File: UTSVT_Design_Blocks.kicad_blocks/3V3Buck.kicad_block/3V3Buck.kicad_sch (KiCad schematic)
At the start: 8 parts, among them U1 LMR51635XDDCR

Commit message: review addressed
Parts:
- C3: P/N 963-T21GCB7225MTPA1J -> CL21F225ZAFNNNE
- C6, C7: P/N 963-MLAST32MAB5476MP -> GRM32ER61C476KE15L
- L1: footprint Inductor_SMD:L_Cenker_CKCS252010 -> Inductor_SMD:L_TDK_SLF6025; LCSC P/N C354546 -> C2997651; P/N 710-78439346056 -> PNLS6045-5R6M 5.6UH
- R6: P/N 652-CR0603FX-3162ELF -> 0603WAF3162T5E
- R7: P/N 603-RT0603DRE0710K2L -> 0603WAF1022T5E
- U1: P/N 595-LMR51635XDDCR -> LMR51635XDDCR
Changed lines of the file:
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@@
 			)
 		)
-		(property "P/N" "963-MLAST32MAB5476MP"
+		(property "P/N" "GRM32ER61C476KE15L"
 			(at 166.37 85.09 0)
 			(effects
@@
 			)
 		)
-		(property "P/N" "652-CR0603FX-3162ELF"
+		(property "P/N" "0603WAF3162T5E"
 			(at 201.93 82.55 0)
 			(effects
@@
 			)
 		)
-		(property "P/N" "963-MLAST32MAB5476MP"
+		(property "P/N" "GRM32ER61C476KE15L"
 			(at 154.94 85.09 0)
 			(effects
@@
 			)
 		)
-		(property "Footprint" "Inductor_SMD:L_Cenker_CKCS252010"
+		(property "Footprint" "Inductor_SMD:L_TDK_SLF6025"
 			(at 146.05 81.28 0)
 			(effects
@@
 			)
 		)
-		(property "LCSC P/N" "C354546"
+		(property "LCSC P/N" "C2997651"
 			(at 146.05 81.28 90)
 			(effects
@@
 			)
 		)
-		(property "P/N" "710-78439346056"
+		(property "P/N" "PNLS6045-5R6M 5.6UH"
 			(at 146.05 81.28 90)
 			(effects
@@
 			)
 		)
-		(property "P/N" "595-LMR51635XDDCR"
+		(property "P/N" "LMR51635XDDCR"
 			(at 97.79 76.2 0)
 			(effects
@@
 			)
 		)
-		(property "P/N" "963-T21GCB7225MTPA1J"
+		(property "P/N" "CL21F225ZAFNNNE"
 			(at 77.47 81.28 0)
 			(effects
@@
 			)
 		)
-		(property "P/N" "603-RT0603DRE0710K2L"
+		(property "P/N" "0603WAF1022T5E"
 			(at 201.93 90.17 0)
 			(effects

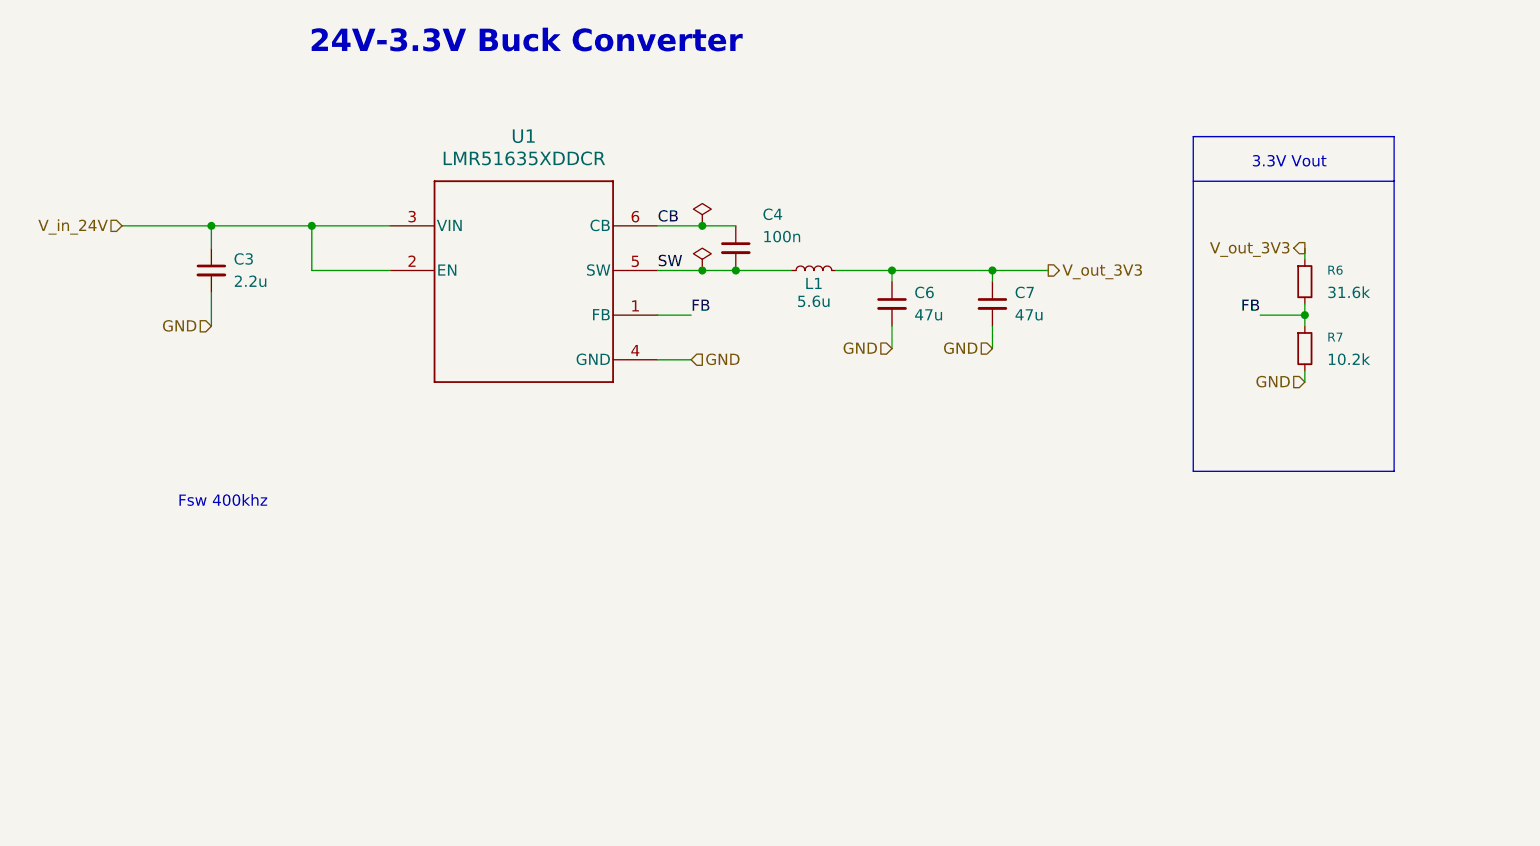
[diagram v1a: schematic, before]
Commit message: fixed designators
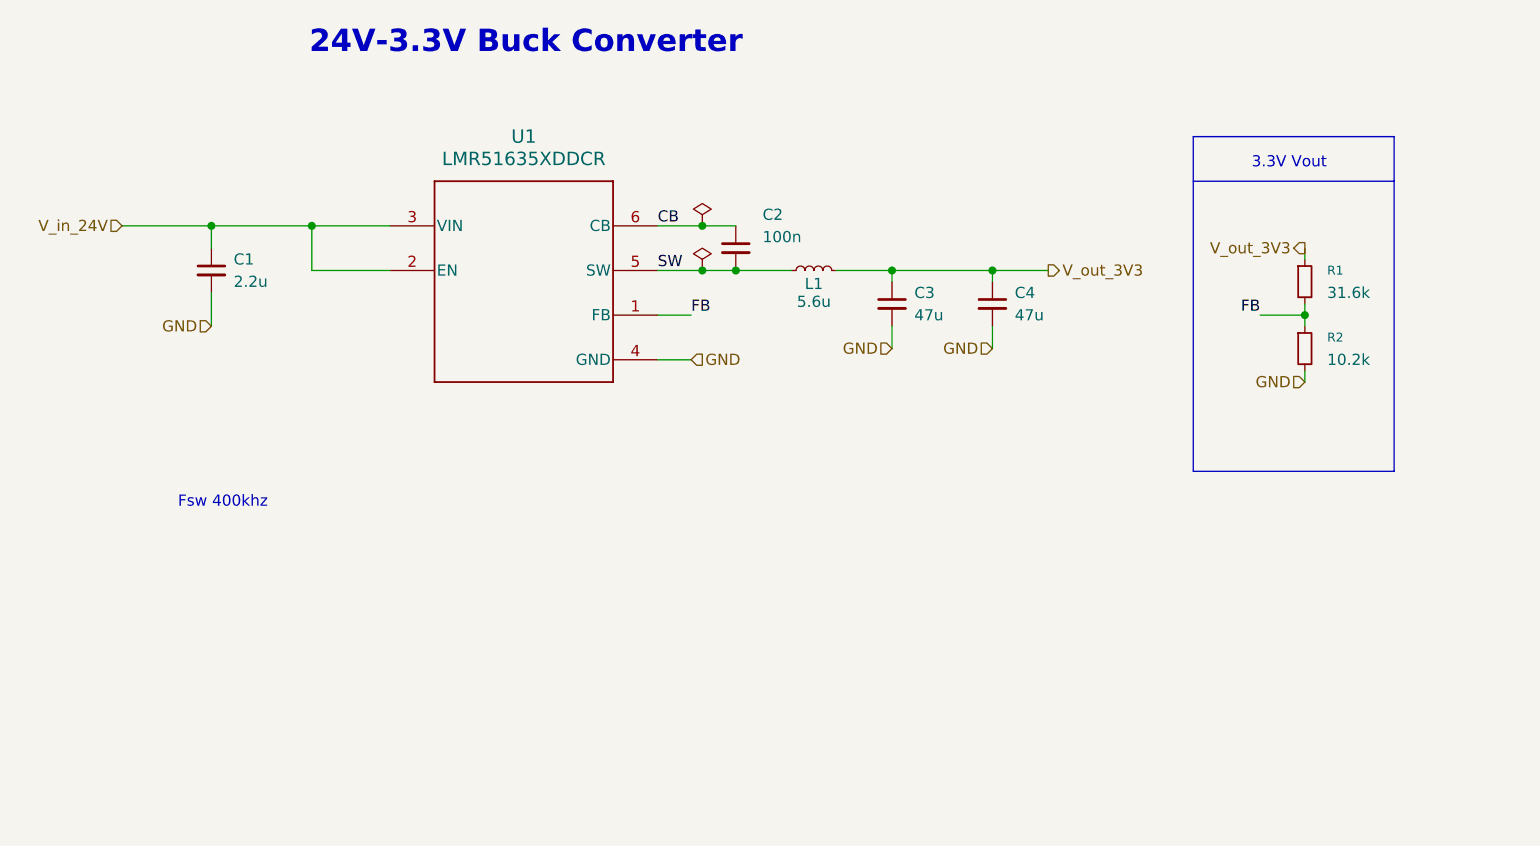
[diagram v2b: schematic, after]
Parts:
- renumbered C3 to C1, C4 to C2, C6 to C3, C7 to C4, R6 to R1, R7 to R2
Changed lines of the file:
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@@
 		(dnp no)
 		(fields_autoplaced yes)
-		(property "Reference" "C7"
+		(property "Reference" "C4"
 			(at 168.91 83.8262 0)
 			(effects
@@
 				(path "/331f457b-ed4e-4d4a-ad6d-c8acb2febfed/5a40936c-0191-464a-8f77-aefefe09d184"
 					(reference "C7")
+					(unit 1)
+				)
+			)
+			(project "3V3Buck"
+				(path "/39da07fa-d2fd-433c-a855-3c74e2086fee"
+					(reference "C4")
 					(unit 1)
 				)
@@
 		(dnp no)
 		(fields_autoplaced yes)
-		(property "Reference" "R6"
+		(property "Reference" "R1"
 			(at 204.47 81.2799 0)
 			(effects
@@
 				(path "/331f457b-ed4e-4d4a-ad6d-c8acb2febfed/5a40936c-0191-464a-8f77-aefefe09d184"
 					(reference "R6")
+					(unit 1)
+				)
+			)
+			(project "3V3Buck"
+				(path "/39da07fa-d2fd-433c-a855-3c74e2086fee"
+					(reference "R1")
 					(unit 1)
 				)
@@
 		(dnp no)
 		(fields_autoplaced yes)
-		(property "Reference" "C6"
+		(property "Reference" "C3"
 			(at 157.48 83.8262 0)
 			(effects
@@
 				(path "/331f457b-ed4e-4d4a-ad6d-c8acb2febfed/5a40936c-0191-464a-8f77-aefefe09d184"
 					(reference "C6")
+					(unit 1)
+				)
+			)
+			(project "3V3Buck"
+				(path "/39da07fa-d2fd-433c-a855-3c74e2086fee"
+					(reference "C3")
 					(unit 1)
 				)
@@
 		(dnp no)
 		(fields_autoplaced yes)
-		(property "Reference" "#FLG04"
+		(property "Reference" "#FLG01"
 			(at 133.35 74.295 0)
 			(effects
@@
 				(path "/331f457b-ed4e-4d4a-ad6d-c8acb2febfed/5a40936c-0191-464a-8f77-aefefe09d184"
 					(reference "#FLG04")
+					(unit 1)
+				)
+			)
+			(project "3V3Buck"
+				(path "/39da07fa-d2fd-433c-a855-3c74e2086fee"
+					(reference "#FLG01")
 					(unit 1)
 				)
@@
 				)
 			)
+			(project "3V3Buck"
+				(path "/39da07fa-d2fd-433c-a855-3c74e2086fee"
+					(reference "L1")
+					(unit 1)
+				)
+			)
 		)
 	)
@@
 				)
 			)
+			(project "3V3Buck"
+				(path "/39da07fa-d2fd-433c-a855-3c74e2086fee"
+					(reference "U1")
+					(unit 1)
+				)
+			)
 		)
 	)
@@
 		(dnp no)
 		(fields_autoplaced yes)
-		(property "Reference" "C3"
+		(property "Reference" "C1"
 			(at 80.01 80.0162 0)
 			(effects
@@
 				(path "/331f457b-ed4e-4d4a-ad6d-c8acb2febfed/5a40936c-0191-464a-8f77-aefefe09d184"
 					(reference "C3")
+					(unit 1)
+				)
+			)
+			(project "3V3Buck"
+				(path "/39da07fa-d2fd-433c-a855-3c74e2086fee"
+					(reference "C1")
 					(unit 1)
 				)
@@
 		(on_board yes)
 		(dnp no)
-		(property "Reference" "#FLG03"
+		(property "Reference" "#FLG02"
 			(at 133.35 79.375 0)
 			(effects
@@
 				(path "/331f457b-ed4e-4d4a-ad6d-c8acb2febfed/5a40936c-0191-464a-8f77-aefefe09d184"
 					(reference "#FLG03")
+					(unit 1)
+				)
+			)
+			(project "3V3Buck"
+				(path "/39da07fa-d2fd-433c-a855-3c74e2086fee"
+					(reference "#FLG02")
 					(unit 1)
 				)
@@
 		(on_board yes)
 		(dnp no)
-		(property "Reference" "C4"
+		(property "Reference" "C2"
 			(at 140.208 74.93 0)
 			(effects
@@
 				(path "/331f457b-ed4e-4d4a-ad6d-c8acb2febfed/5a40936c-0191-464a-8f77-aefefe09d184"
 					(reference "C4")
+					(unit 1)
+				)
+			)
+			(project "3V3Buck"
+				(path "/39da07fa-d2fd-433c-a855-3c74e2086fee"
+					(reference "C2")
 					(unit 1)
 				)
@@
 		(dnp no)
 		(fields_autoplaced yes)
-		(property "Reference" "R7"
+		(property "Reference" "R2"
 			(at 204.47 88.8999 0)
 			(effects
@@
 				)
 			)
-		)
-	)
+			(project "3V3Buck"
+				(path "/39da07fa-d2fd-433c-a855-3c74e2086fee"
+					(reference "R2")
+					(unit 1)
+				)
+			)
+		)
+	)
+	(sheet_instances
+		(path "/"
+			(page "1")
+		)
+	)
+	(embedded_fonts no)
 )

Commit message: updated 12V/3V buck resistor footprint + added test points (#57)
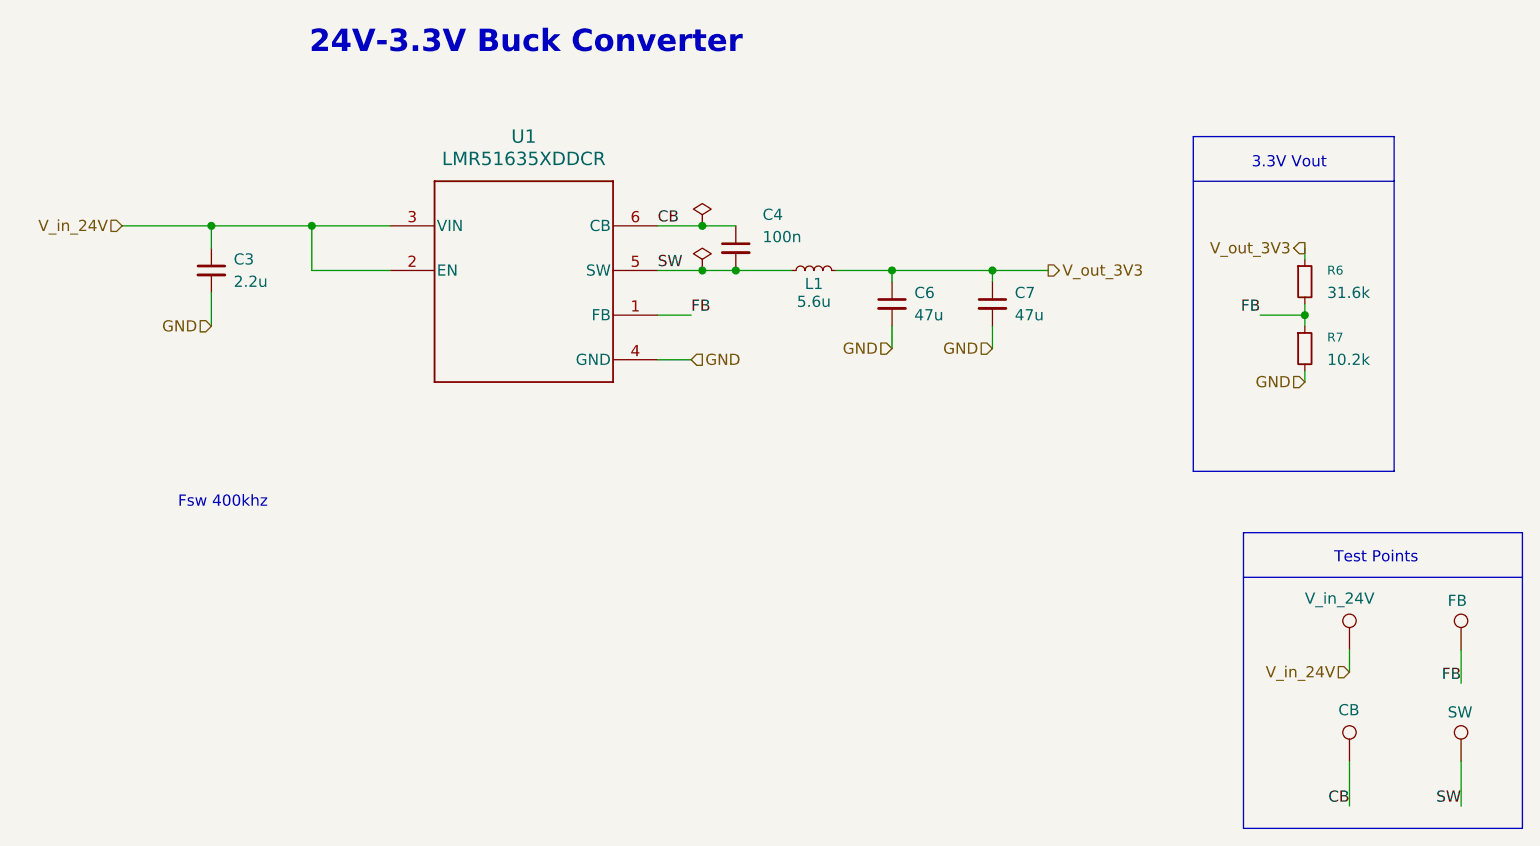
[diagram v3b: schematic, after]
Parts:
- added TP16: V_in_24V, TestPoint:TestPoint_THTPad_D3.0mm_Drill1.5mm, symbol Connector:TestPoint
- added TP17: CB, TestPoint:TestPoint_THTPad_D3.0mm_Drill1.5mm, symbol Connector:TestPoint
- added TP18: FB, TestPoint:TestPoint_THTPad_D3.0mm_Drill1.5mm, symbol Connector:TestPoint
- added TP19: SW, TestPoint:TestPoint_THTPad_D3.0mm_Drill1.5mm, symbol Connector:TestPoint
- R6: renamed from R1; footprint Resistor_SMD:R_0201_0603Metric_Pad0.64x0.40mm_HandSolder -> Resistor_SMD:R_0603_1608Metric
- R7: renamed from R2; footprint Resistor_SMD:R_0201_0603Metric_Pad0.64x0.40mm_HandSolder -> Resistor_SMD:R_0603_1608Metric
- renumbered C1 to C3, C2 to C4, C3 to C6, C4 to C7
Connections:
- net CB: now also TP17.1
- net FB: now also TP18.1
- net SW: now also TP19.1
- net V_in_24V: now also TP16.1
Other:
- note added: "Test Points"
